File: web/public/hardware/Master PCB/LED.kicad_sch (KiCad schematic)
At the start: 12 parts, among them Q1 2N7000, Q2 2N7000, Q3 2N7000, Q4 2N7000

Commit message: Finish schematic and start routing PCB
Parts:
- R10, R11, R12, R13, R14, R15, R16, R17: footprint (none) -> Resistor_SMD:R_0805_2012Metric_Pad1.20x1.40mm_HandSolder
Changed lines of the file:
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@@
       (effects (font (size 1.27 1.27)) (justify left))
     )
-    (property "Footprint" "" (at 147.32 132.08 0)
+    (property "Footprint" "Resistor_SMD:R_0805_2012Metric_Pad1.20x1.40mm_HandSolder" (at 147.32 132.08 0)
       (effects (font (size 1.27 1.27)) hide)
     )
@@
       (effects (font (size 1.27 1.27)) (justify left))
     )
-    (property "Footprint" "" (at 125.73 81.28 0)
+    (property "Footprint" "Resistor_SMD:R_0805_2012Metric_Pad1.20x1.40mm_HandSolder" (at 125.73 81.28 0)
       (effects (font (size 1.27 1.27)) hide)
     )
@@
       (effects (font (size 1.27 1.27)) (justify left))
     )
-    (property "Footprint" "" (at 125.73 132.08 0)
+    (property "Footprint" "Resistor_SMD:R_0805_2012Metric_Pad1.20x1.40mm_HandSolder" (at 125.73 132.08 0)
       (effects (font (size 1.27 1.27)) hide)
     )
@@
       (effects (font (size 1.27 1.27)) (justify left))
     )
-    (property "Footprint" "" (at 125.73 55.88 0)
+    (property "Footprint" "Resistor_SMD:R_0805_2012Metric_Pad1.20x1.40mm_HandSolder" (at 125.73 55.88 0)
       (effects (font (size 1.27 1.27)) hide)
     )
@@
       (effects (font (size 1.27 1.27)) (justify left))
     )
-    (property "Footprint" "" (at 147.32 106.68 0)
+    (property "Footprint" "Resistor_SMD:R_0805_2012Metric_Pad1.20x1.40mm_HandSolder" (at 147.32 106.68 0)
       (effects (font (size 1.27 1.27)) hide)
     )
@@
       (effects (font (size 1.27 1.27)) (justify left))
     )
-    (property "Footprint" "" (at 125.73 106.68 0)
+    (property "Footprint" "Resistor_SMD:R_0805_2012Metric_Pad1.20x1.40mm_HandSolder" (at 125.73 106.68 0)
       (effects (font (size 1.27 1.27)) hide)
     )
@@
       (effects (font (size 1.27 1.27)) (justify left))
     )
-    (property "Footprint" "" (at 147.32 81.28 0)
+    (property "Footprint" "Resistor_SMD:R_0805_2012Metric_Pad1.20x1.40mm_HandSolder" (at 147.32 81.28 0)
       (effects (font (size 1.27 1.27)) hide)
     )
@@
       (effects (font (size 1.27 1.27)) (justify left))
     )
-    (property "Footprint" "" (at 147.32 55.88 0)
-      (effects (font (size 1.27 1.27)) hide)
-    )
+    (property "Footprint" "Resistor_SMD:R_0805_2012Metric_Pad1.20x1.40mm_HandSolder" (at 147.32 55.88 0)
+      (effects (font (size 1.27 1.27)) hide)
+    )

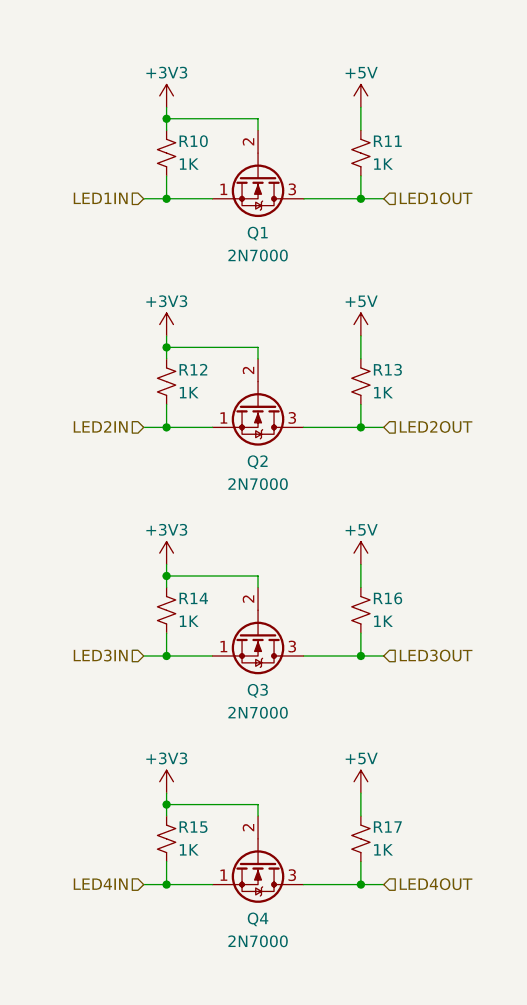
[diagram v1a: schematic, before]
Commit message: Finish routing Master PCB, create sensor PCB project
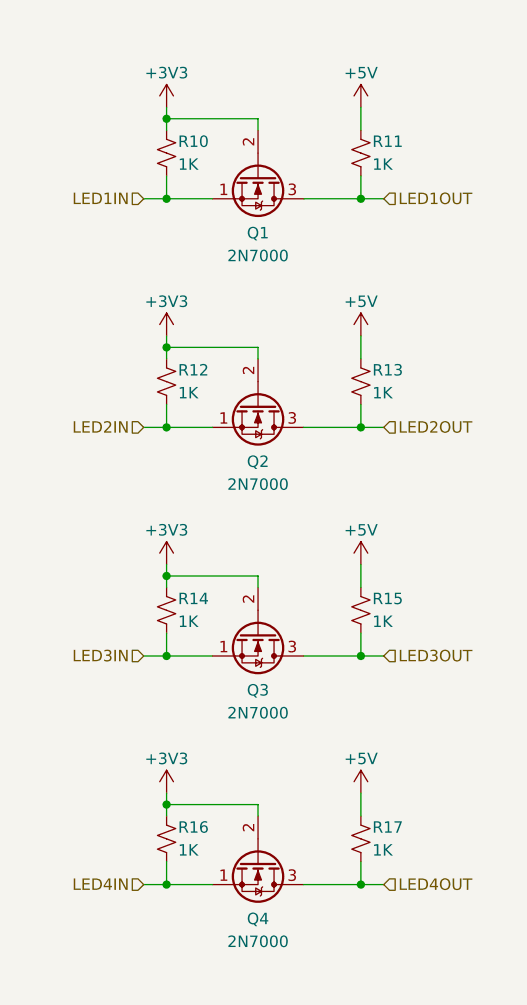
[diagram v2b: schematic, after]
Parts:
- renumbered R16 to R15, R15 to R16
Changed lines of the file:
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@@
   (symbol (lib_id "Device:R_Small_US") (at 125.73 132.08 0) (unit 1)
     (in_bom yes) (on_board yes) (dnp no)
-    (property "Reference" "R15" (at 127 130.81 0)
+    (property "Reference" "R16" (at 127 130.81 0)
       (effects (font (size 1.27 1.27)) (justify left))
     )
@@
       (project "Master PCB"
         (path "/61606422-4f73-4717-9ce6-6ac5e634e7ae/8e455560-fe02-4a1f-aeeb-dbc2a430fc5a"
-          (reference "R15") (unit 1)
+          (reference "R16") (unit 1)
         )
       )
@@
   (symbol (lib_id "Device:R_Small_US") (at 147.32 106.68 0) (unit 1)
     (in_bom yes) (on_board yes) (dnp no)
-    (property "Reference" "R16" (at 148.59 105.41 0)
+    (property "Reference" "R15" (at 148.59 105.41 0)
       (effects (font (size 1.27 1.27)) (justify left))
     )
@@
       (project "Master PCB"
         (path "/61606422-4f73-4717-9ce6-6ac5e634e7ae/8e455560-fe02-4a1f-aeeb-dbc2a430fc5a"
-          (reference "R16") (unit 1)
+          (reference "R15") (unit 1)
         )
       )

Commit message: More misc. cleanup and generate updated production files
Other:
- note added: "LED level shifters"
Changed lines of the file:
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@@
     (stroke (width 0) (type default))
+  )
+  (rectangle (start 109.22 43.18) (end 163.83 148.59)
+    (stroke (width 0) (type default))
+    (fill (type none))
+  )
+  (text "LED level shifters" (at 109.22 43.18 0)
+    (effects (font (size 1.27 1.27)) (justify left bottom))
   )
   (hierarchical_label "LED4IN" (shape input) (at 123.19 137.16 180) (fields_autoplaced)
